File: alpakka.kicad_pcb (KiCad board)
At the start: 2 copper layers, 130 x 51 mm, 94 parts, among them P1 Debug, P2 Endpoint, P3 Conn_01x02, Q1 Q_PMOS_DGS, U1 Raspberry_Pico, U10 ST_LSM6, U12 ST_LSM6, U2 Alpsalpine_RKJXV, U3 Alpsalpine_EC10E, U4 Alpsalpine_RKJXM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

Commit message: Bump version for incomming release
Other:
- board text added: "b0.90.0"
- board text removed: "b0.88.0"
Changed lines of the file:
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@@
     (effects (font (size 1 1) (thickness 0.16)) (justify left))
   )
-  (gr_text "b0.88.0" (at 99.2 81.75) (layer "F.SilkS")
+  (gr_text "b0.90.0" (at 99.2 81.75) (layer "F.SilkS")
     (effects (font (size 1 1) (thickness 0.16)) (justify left))
   )

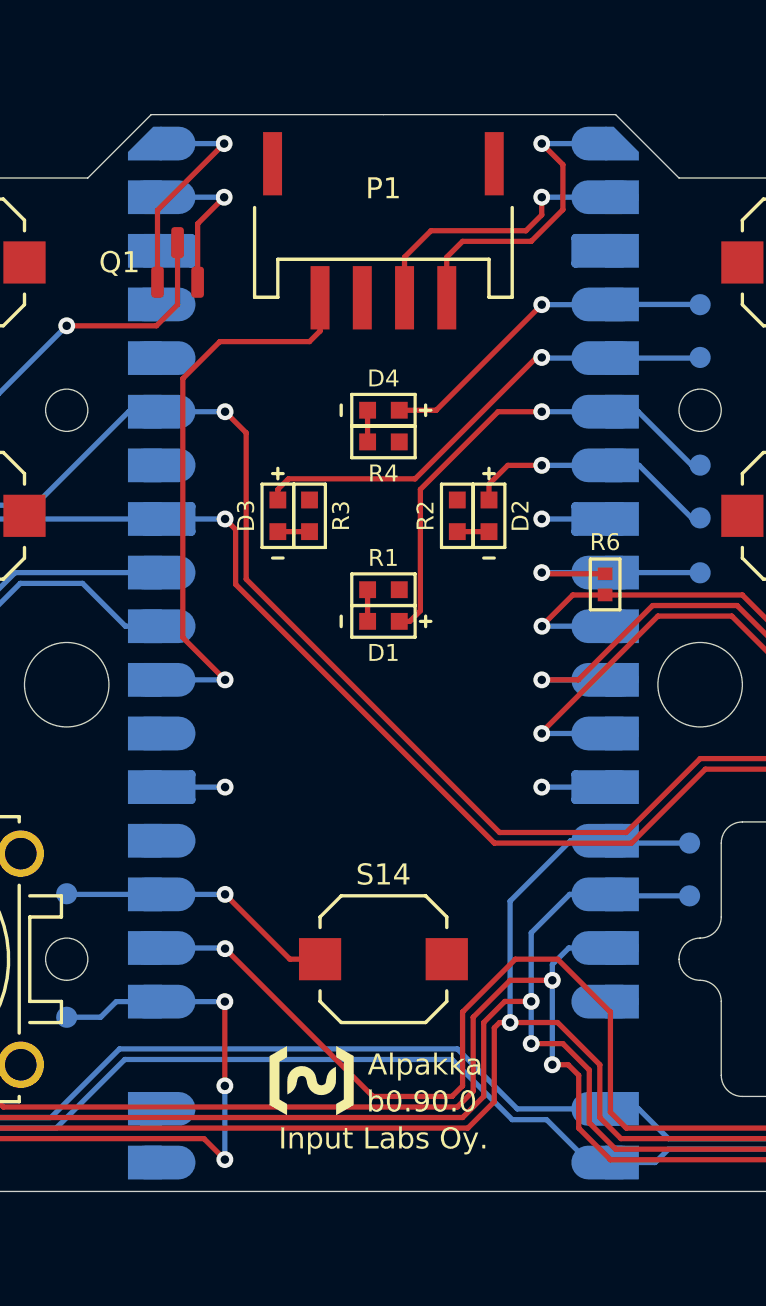
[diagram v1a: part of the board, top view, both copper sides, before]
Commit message: Changed JST connector, Added Mount and Export properties, Tweaked components origins
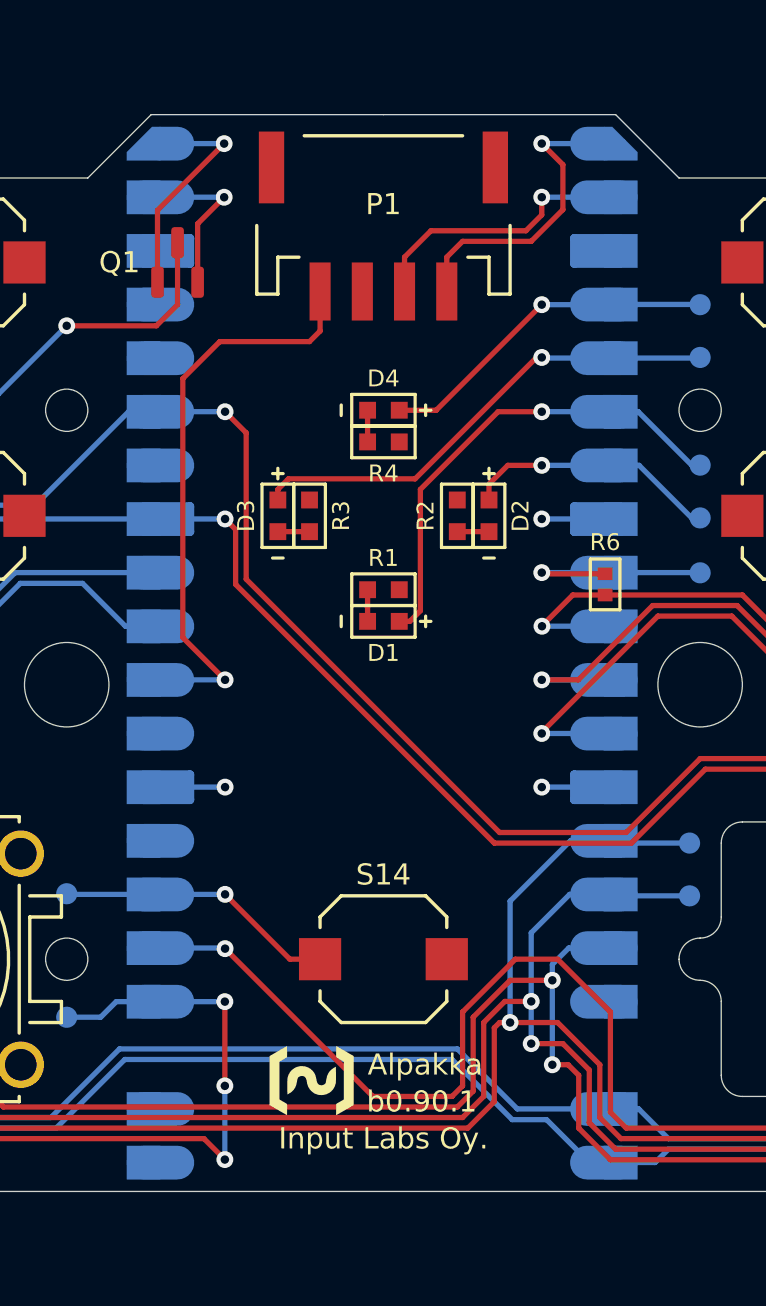
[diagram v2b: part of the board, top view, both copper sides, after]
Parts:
- P1: footprint ILO_fp:Boomele_C50137 -> ILO_fp:JST_S4B-PH-SM4-K-TB
- moved U3 1.00 mm to (127.0, 74.5)
- moved U1 0.41 mm to (100.0, 60.9), turned to -90 degrees
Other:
- board text added: "b0.90.1"
- board text removed: "b0.90.0"

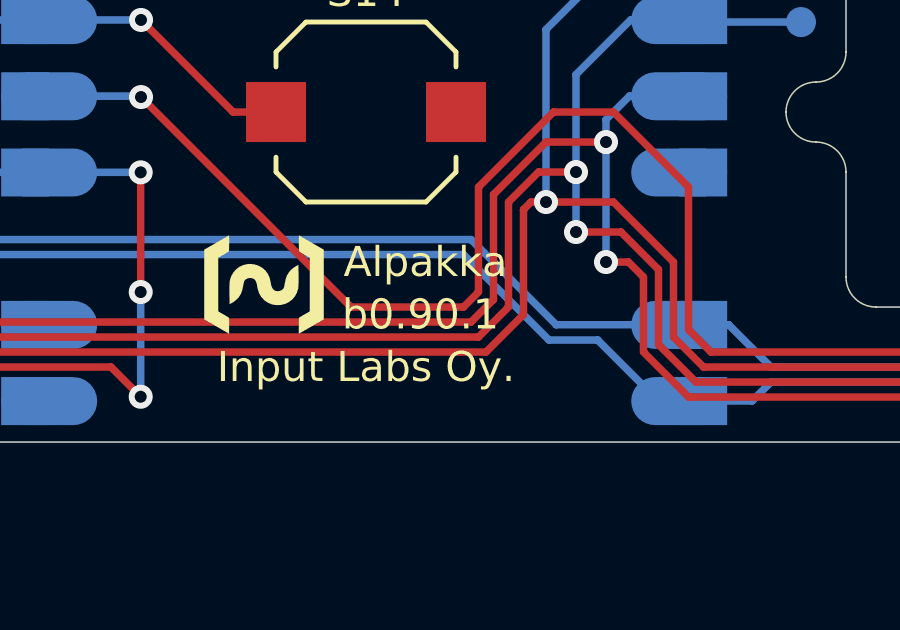
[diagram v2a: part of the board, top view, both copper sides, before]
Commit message: Added silk labels for pico soldering
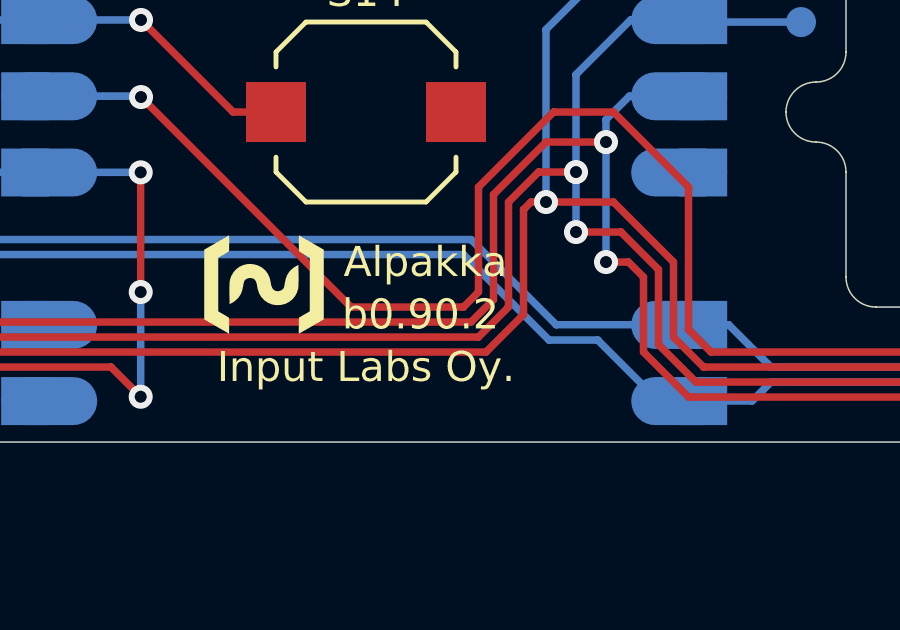
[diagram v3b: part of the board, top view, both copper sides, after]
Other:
- board text added: "USB UP"
- board text added: "b0.90.2"
- board text removed: "b0.90.1"
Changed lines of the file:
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@@
   (gr_line (start 152.853553 73) (end 153.25 73)
     (stroke (width 0.16) (type solid)) (layer "B.SilkS"))
+  (gr_line (start 100.5 41.25) (end 100.5 41)
+    (stroke (width 0.16) (type default)) (layer "B.SilkS"))
   (gr_line (start 120.25 39.5) (end 118.75 39.5)
     (stroke (width 0.16) (type solid)) (layer "B.SilkS"))
+  (gr_line (start 99.5 44.5) (end 100.5 44.5)
+    (stroke (width 0.16) (type default)) (layer "B.SilkS"))
   (gr_line (start 47.853553 73) (end 48.25 73)
     (stroke (width 0.16) (type solid)) (layer "B.SilkS"))
@@
   (gr_circle (center 152.5 73) (end 152.25 73.25)
     (stroke (width 0.16) (type solid)) (fill none) (layer "B.SilkS"))
+  (gr_line (start 100.5 44.5) (end 100.5 43.5)
+    (stroke (width 0.16) (type default)) (layer "B.SilkS"))
+  (gr_line (start 101 43.5) (end 100 42.5)
+    (stroke (width 0.16) (type default)) (layer "B.SilkS"))
   (gr_line (start 155 54.353553) (end 155 54.75)
     (stroke (width 0.16) (type solid)) (layer "B.SilkS"))
@@
   (gr_line (start 45 54.353553) (end 45 54.75)
     (stroke (width 0.16) (type solid)) (layer "B.SilkS"))
+  (gr_line (start 102.5 36) (end 102.75 36.5)
+    (stroke (width 0.16) (type default)) (layer "B.SilkS"))
   (gr_rect (start 119 41.5) (end 119.5 42)
     (stroke (width 0.16) (type solid)) (fill solid) (layer "B.SilkS"))
+  (gr_line (start 97.5 36) (end 102.5 36)
+    (stroke (width 0.16) (type default)) (layer "B.SilkS"))
   (gr_rect (start 115.25 41.5) (end 115.75 42)
     (stroke (width 0.16) (type solid)) (fill solid) (layer "B.SilkS"))
   (gr_line (start 114.5 42.75) (end 120.25 42.75)
     (stroke (width 0.16) (type solid)) (layer "B.SilkS"))
+  (gr_line (start 103 36.5) (end 103.25 36)
+    (stroke (width 0.16) (type default)) (layer "B.SilkS"))
   (gr_line (start 116 38.75) (end 116 39.5)
     (stroke (width 0.16) (type solid)) (layer "B.SilkS"))
+  (gr_rect (start 101.5 37.5) (end 102 38.5)
+    (stroke (width 0.16) (type default)) (fill none) (layer "B.SilkS"))
+  (gr_line (start 99.5 43.5) (end 99.5 44.5)
+    (stroke (width 0.16) (type default)) (layer "B.SilkS"))
+  (gr_line (start 100 41.25) (end 100 41)
+    (stroke (width 0.16) (type default)) (layer "B.SilkS"))
   (gr_line (start 118.75 38.75) (end 116 38.75)
     (stroke (width 0.16) (type solid)) (layer "B.SilkS"))
+  (gr_line (start 100 42.5) (end 99 43.5)
+    (stroke (width 0.16) (type default)) (layer "B.SilkS"))
+  (gr_line (start 99.5 41.25) (end 99.5 41)
+    (stroke (width 0.16) (type default)) (layer "B.SilkS"))
+  (gr_line (start 100.5 43.5) (end 101 43.5)
+    (stroke (width 0.16) (type default)) (layer "B.SilkS"))
   (gr_line (start 155 53.646447) (end 155 53.25)
     (stroke (width 0.16) (type solid)) (layer "B.SilkS"))
+  (gr_circle (center 106 36.3728) (end 106.353553 36.3728)
+    (stroke (width 0.16) (type solid)) (fill solid) (layer "B.SilkS"))
+  (gr_rect (start 97 36.5) (end 103 40.75)
+    (stroke (width 0.16) (type default)) (fill none) (layer "B.SilkS"))
   (gr_line (start 152.146447 73) (end 151.75 73)
     (stroke (width 0.16) (type solid)) (layer "B.SilkS"))
+  (gr_line (start 101 41.25) (end 101 41)
+    (stroke (width 0.16) (type default)) (layer "B.SilkS"))
   (gr_line (start 120.25 42.75) (end 120.25 39.5)
     (stroke (width 0.16) (type solid)) (layer "B.SilkS"))
+  (gr_line (start 99 41.25) (end 99 41)
+    (stroke (width 0.16) (type default)) (layer "B.SilkS"))
+  (gr_line (start 97.25 36.5) (end 97.5 36)
+    (stroke (width 0.16) (type default)) (layer "B.SilkS"))
+  (gr_line (start 99 43.5) (end 99.5 43.5)
+    (stroke (width 0.16) (type default)) (layer "B.SilkS"))
   (gr_line (start 118.75 39.5) (end 118.75 38.75)
     (stroke (width 0.16) (type solid)) (layer "B.SilkS"))
+  (gr_rect (start 98 37.5) (end 98.5 38.5)
+    (stroke (width 0.16) (type default)) (fill none) (layer "B.SilkS"))
   (gr_circle (center 45 54) (end 45.25 54.25)
     (stroke (width 0.16) (type solid)) (fill none) (layer "B.SilkS"))
@@
   (gr_rect (start 116.5 41.5) (end 117 42)
     (stroke (width 0.16) (type solid)) (fill solid) (layer "B.SilkS"))
+  (gr_line (start 97 36.5) (end 96.75 36)
+    (stroke (width 0.16) (type default)) (layer "B.SilkS"))
   (gr_arc (start 162.75 82.75) (mid 163.221847 82.868345) (end 163.58205 83.1953)
     (stroke (width 0.153) (type solid)) (layer "F.SilkS"))
@@
     (effects (font (size 0.8 0.8) (thickness 0.153)) (justify mirror))
   )
+  (gr_text "USB\nUP" (at 100 46.5) (layer "B.SilkS")
+    (effects (font (size 1 1) (thickness 0.16)) (justify mirror))
+  )
   (gr_text "34" (at 86.8 51.6 270) (layer "B.SilkS")
     (effects (font (size 0.8 0.8) (thickness 0.153)) (justify mirror))
@@
   )
   (gr_text "38\n" (at 86.75 41.5 270) (layer "B.SilkS")
+    (effects (font (size 0.8 0.8) (thickness 0.153)) (justify mirror))
+  )
+  (gr_text "1" (at 104.7496 36.3728) (layer "B.SilkS")
     (effects (font (size 0.8 0.8) (thickness 0.153)) (justify mirror))
   )
@@
     (effects (font (size 1 1) (thickness 0.16)) (justify left))
   )
-  (gr_text "b0.90.1" (at 99.2 81.75) (layer "F.SilkS")
+  (gr_text "b0.90.2" (at 99.2 81.75) (layer "F.SilkS")
     (effects (font (size 1 1) (thickness 0.16)) (justify left))
   )
